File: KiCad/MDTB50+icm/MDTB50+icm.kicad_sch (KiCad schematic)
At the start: 21 parts, among them U1 ICM-45686

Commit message: - DIY PCB fully routed. But it kinda sucks.
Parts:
- renumbered U3 to TP1
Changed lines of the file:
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@@
 		(on_board yes)
 		(dnp no)
-		(property "Reference" "U3"
+		(property "Reference" "TP1"
 			(at 52.07 35.052 0)
 			(effects
@@
 			(project ""
 				(path "/fc39c71d-b4a8-40e7-814c-897ce106e5ba"
-					(reference "U3")
+					(reference "TP1")
 					(unit 1)
 				)

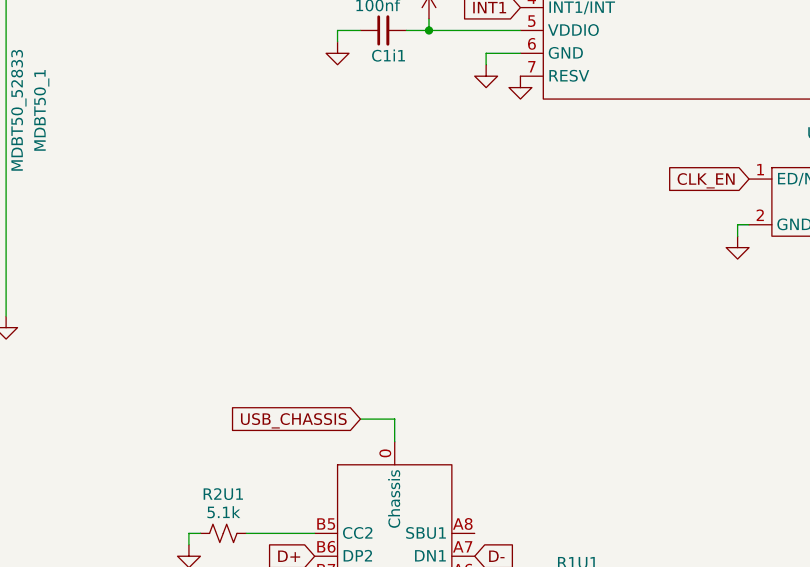
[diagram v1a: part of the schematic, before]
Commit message: - Changed PCB to 4 layer - Added QMC6309 magnetometer
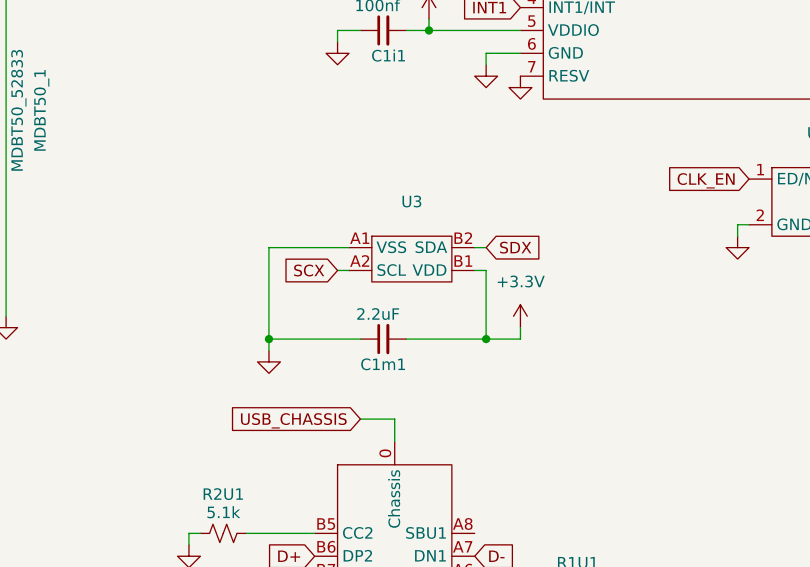
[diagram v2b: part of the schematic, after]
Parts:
- added C1m1: 2.2uF, passive_custom:C_0402_JLC, symbol Device:C_Small
- added U3: ~, mag_custom:QMC6309, symbol mag_custom:QMC6309
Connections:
- net +3.3V: now also C1m1.2, U3.B1 (VDD)
- net GND: now also C1m1.1, U3.A1 (VSS)
- net SCX: now also U3.A2 (SCL)
- net SDX: now also U3.B2 (SDA)

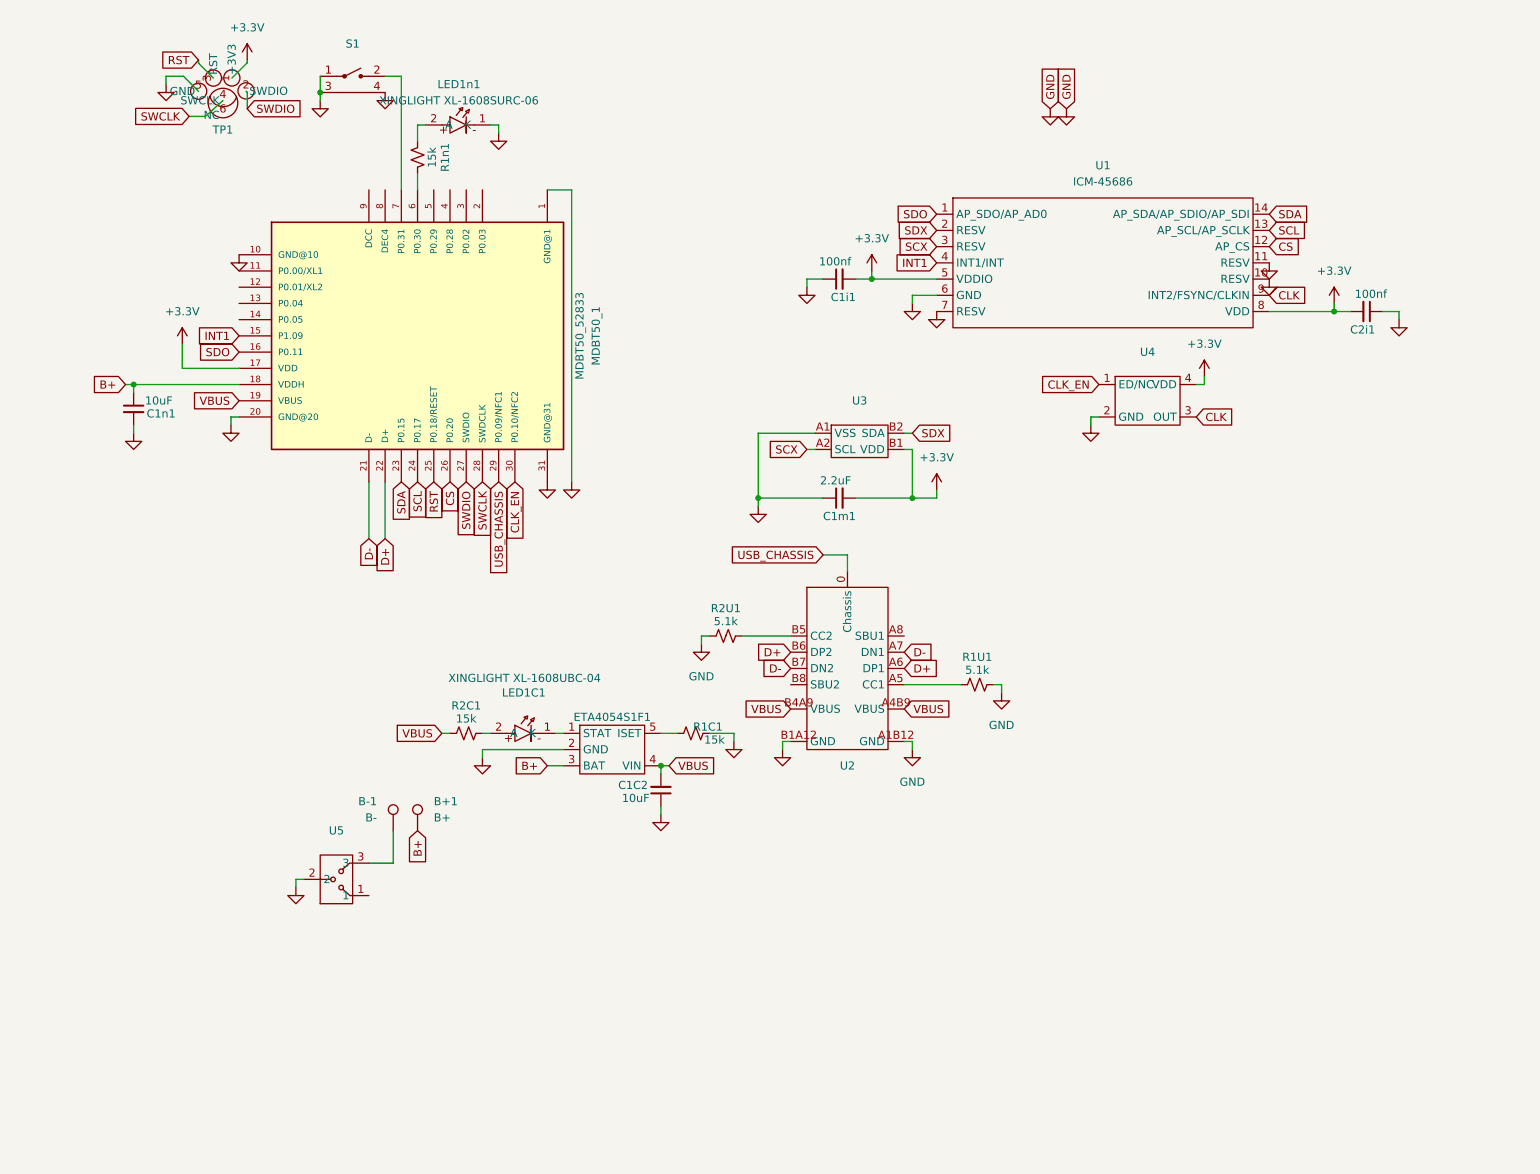
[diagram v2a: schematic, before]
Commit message: - Added external 1.8v regulator, external 3.3v regulator, QMC6309, logic   level shifter for QMC6309, pushbutton power disconnect - Replaced USB C port for better one
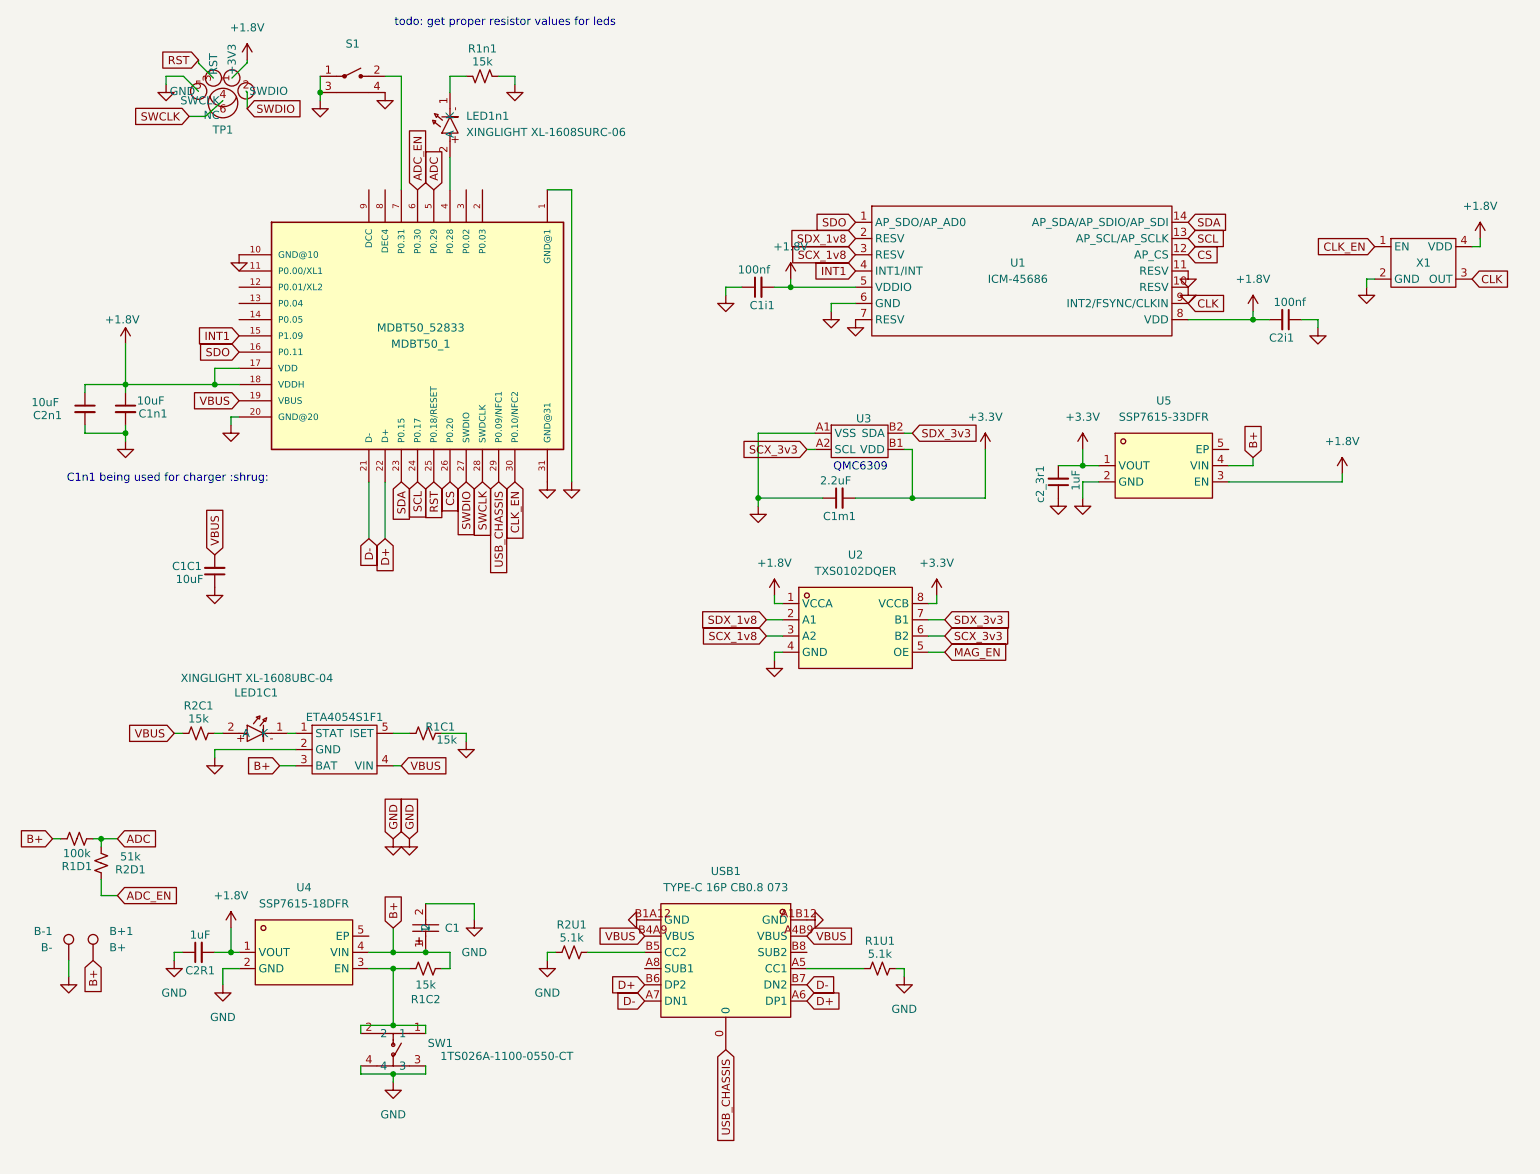
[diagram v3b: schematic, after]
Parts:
- removed C1C2: 10uF, passive_custom:C_0402_JLC, symbol Device:C_Small
- removed U2: ~, USB-C_Custom:HCTL HC-TYPE-C-16P-CB1.0, symbol USB-C_custom:HCTL_HC-TYPE-C-16P-CB1.0
- removed U4: ~, oscillator_custom:HCI 1532H4-32K768JWPDTSNL, symbol oscillator_custom:HCI_1532H4-32K768JWPDTSNL
- removed U5: ~, Switch_Custom:CJS-1200TB, symbol switch-Custom2:Nidec_CJS-1200TB
- added C1: TAJA105K016RNJ, easyeda2kicad:CASE-A_3216, symbol easyeda2kicad:TAJA105K016RNJ
- added C1C1, C2n1: 10uF, passive_custom:C_0402_JLC, symbol Device:C_Small
- added C2R1, c2_3r1: 1uF, passive_custom:C_0402_JLC, symbol Device:C_Small
- added R1C2: 15k, passive_custom:R_0402_JLC, symbol Device:R_Small_US
- added R1D1: 100k, passive_custom:R_0402_JLC, symbol Device:R_Small_US
- added R2D1: 51k, passive_custom:R_0402_JLC, symbol Device:R_Small_US
- added SW1: 1TS026A-1100-0550-CT, easyeda2kicad:SW-SMD_4P-L2.6-W1.6-P0.75-LS3.0, symbol easyeda2kicad:1TS026A-1100-0550-CT
- added U2: TXS0102DQER, Package_SON:X2SON-8_1.4x1mm_P0.35mm, symbol easyeda2kicad:TXS0102DQER
- added U4: SSP7615-18DFR, easyeda2kicad:DFN-4_L1.0-W1.0-P0.65-BL-EP, symbol easyeda2kicad:SSP7615-18DFR
- added U5: SSP7615-33DFR, easyeda2kicad:DFN-4_L1.0-W1.0-P0.65-BL-EP, symbol easyeda2kicad:SSP7615-33DFR
- added USB1: TYPE-C 16P CB0.8 073, easyeda2kicad:USB-C-SMD_TYPE-C-16P-CB0.8-073, symbol easyeda2kicad:TYPE-C16PCB0.8073
- added X1: ~, Crystal:Crystal_SMD_2520-4Pin_2.5x2.0mm, symbol oscillator_custom:SX2M32.768KM20F30TNN
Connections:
- net +3.3V: now also U2.8 (VCCB), U5.1 (VOUT), c2_3r1.2; no longer C1i1.2, C2i1.2, MDBT50_1.17 (VDD), TP1.1 (+3V3), U1.5 (VDDIO), U1.8 (VDD)
- net B+: now also C1.1, R1C2.2, R1D1.2, U4.4 (VIN), U5.4 (VIN); no longer C1n1.1, MDBT50_1.18 (VDDH)
- net CLK: now also X1.3 (OUT)
- net CLK_EN: now also X1.1 (EN)
- net D+: now also USB1.A6 (DP1), USB1.B6 (DP2)
- net D-: now also USB1.A7 (DN1), USB1.B7 (DN2)
- net GND: now also B-1.1, R1n1.1, C1.2, C1C1.1, C2R1.1, C2n1.2, SW1.3, SW1.4, U2.4 (GND), U4.2 (GND), U5.2 (GND), USB1.A1B12 (GND), USB1.B1A12 (GND), X1.2 (GND), c2_3r1.1; no longer LED1n1.1 (K)
- net USB_CHASSIS: now also USB1.0
- net VBUS: now also C1C1.2, USB1.A4B9 (VBUS), USB1.B4A9 (VBUS)
- net at R1U1.1: now also USB1.A5 (CC1)
- net at R2U1.2: now also USB1.B5 (CC2)
- net at MDBT50_1.4 (P0.28): now also LED1n1.2 (A)
- net ADC: now reaches MDBT50_1.5 (P0.29)
- net ADC: now also R1D1.1, R2D1.2
- net ADC_EN: now reaches MDBT50_1.6 (P0.30)
- net ADC_EN: now also R2D1.1; no longer R1n1.1
- net at R1n1.2: now also LED1n1.1 (K); no longer LED1n1.2 (A)
- net SCX renamed SCX_1v8
- net SCX_1v8: now also U2.3 (A2); no longer U3.A2 (SCL)
- net SDX renamed SDX_1v8
- net SDX_1v8: now also U2.2 (A1); no longer U3.B2 (SDA)
- new net: R1C2.1, SW1.1, SW1.2, U4.3 (EN)
- new net +1.8V: C1i1.2, C1n1.1, C2R1.2, C2i1.2, C2n1.1, MDBT50_1.17 (VDD), MDBT50_1.18 (VDDH), TP1.1 (+3V3), U1.5 (VDDIO), U1.8 (VDD), U2.1 (VCCA), U4.1 (VOUT), U5.3 (EN), X1.4 (VDD)
- new net MAG_EN: U2.5 (OE)
- new net SCX_3v3: U2.6 (B2), U3.A2 (SCL)
- new net SDX_3v3: U2.7 (B1), U3.B2 (SDA)
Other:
- note added: "C1n1 being used for charger :shrug:"
- note added: "QMC6309"
- note added: "todo: get proper resistor values for leds"
- moved on the sheet: B+1, B-1, C1i1, C1n1, C2i1, ETA4054S1F1, LED1C1, LED1n1, R1C1, R2C1, U1

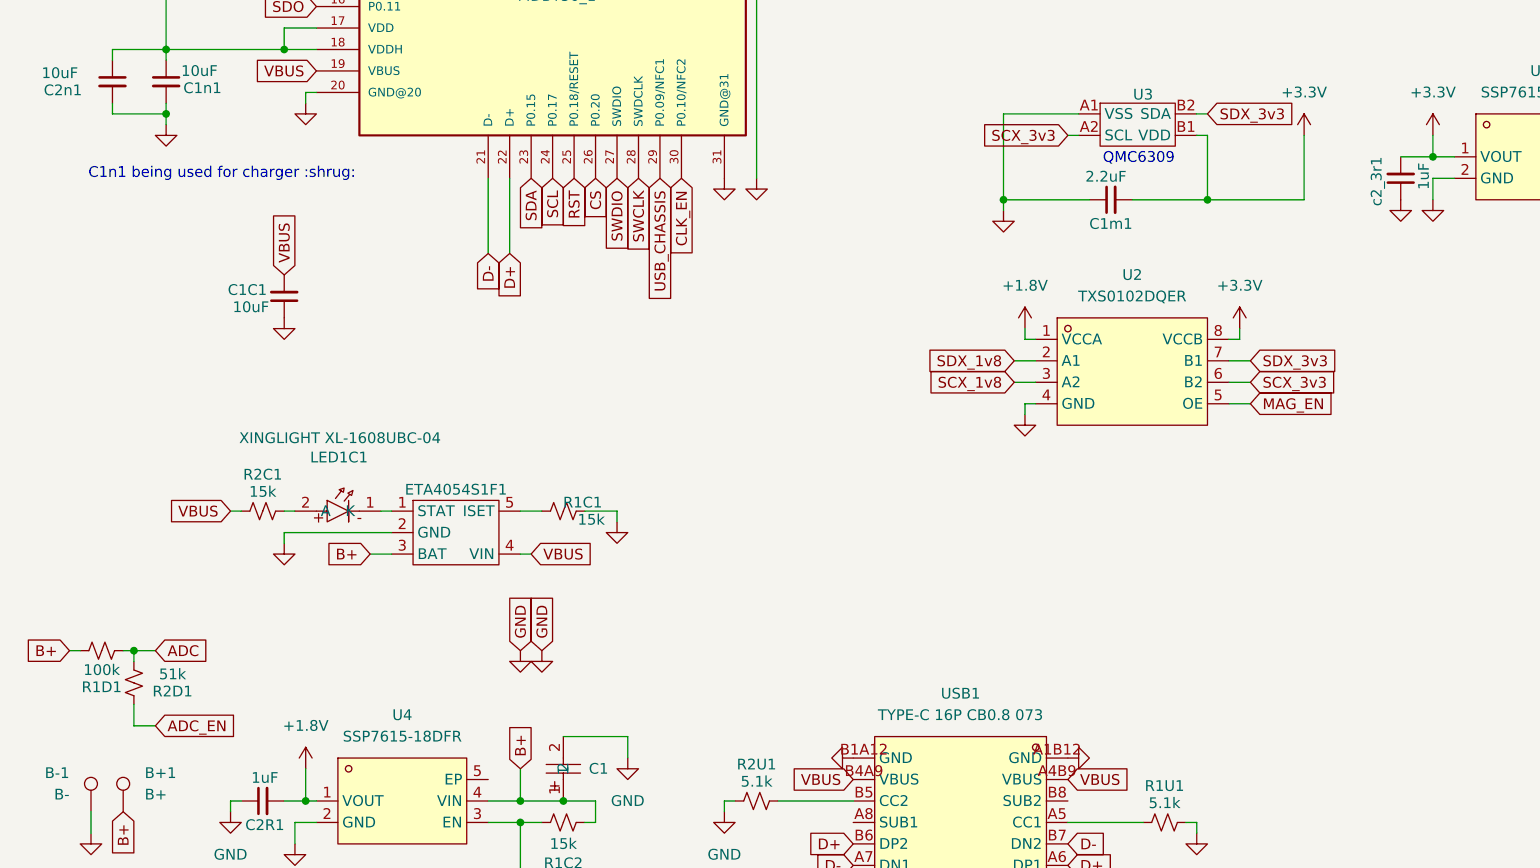
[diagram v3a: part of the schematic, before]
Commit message: - Added ESD protection
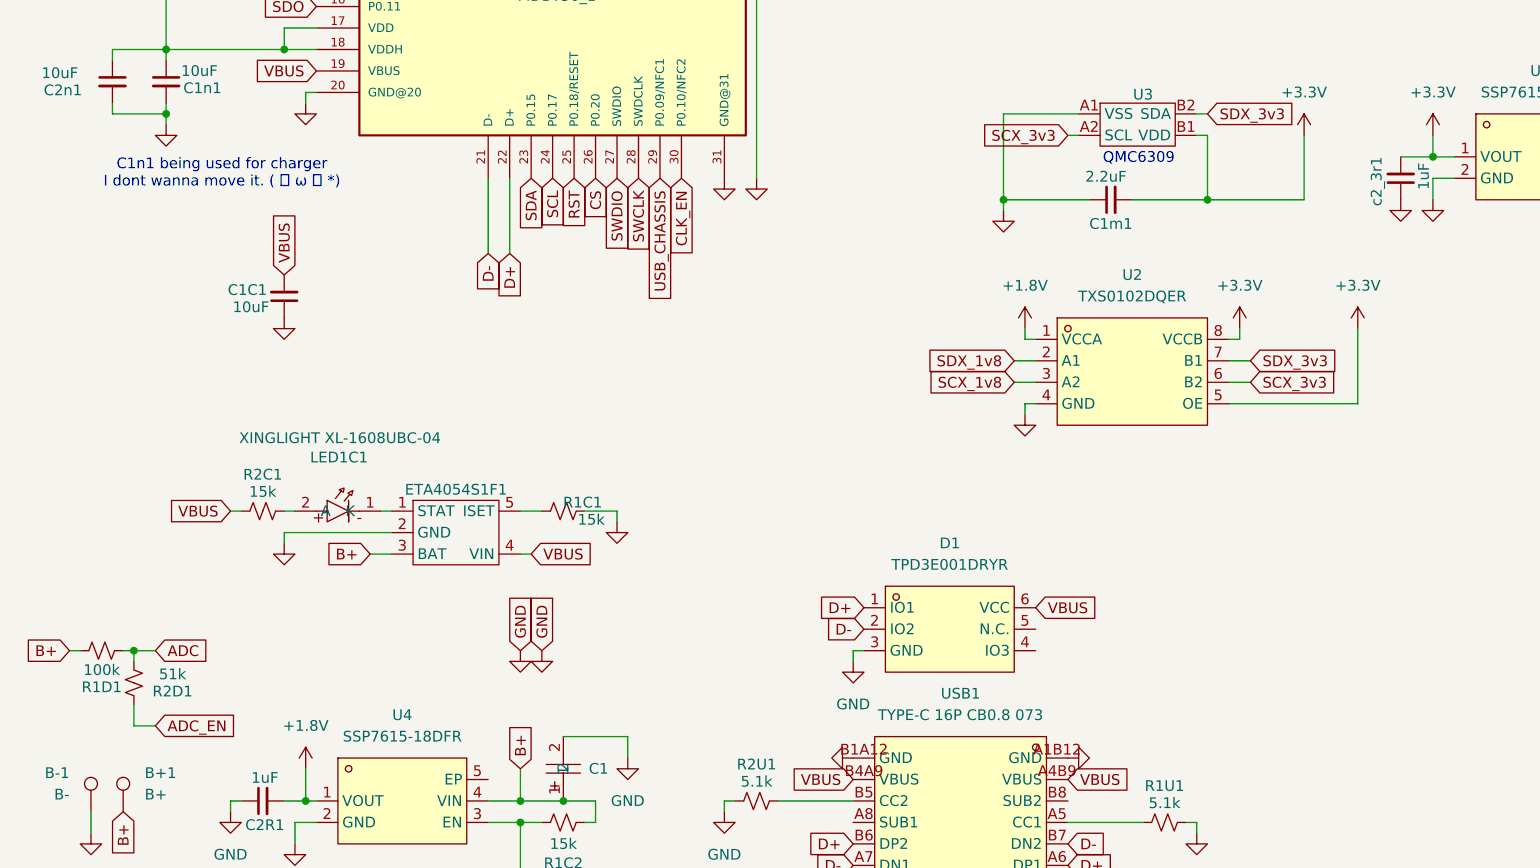
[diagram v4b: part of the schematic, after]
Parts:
- added D1: TPD3E001DRYR, easyeda2kicad:SON-6_L1.5-W1.0-P0.50-BL_SN74LVC1G19DRYR, symbol easyeda2kicad:TPD3E001DRYR
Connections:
- net MAG_EN is gone; now on net +3.3V: U2.5 (OE)
- net D+: now also D1.1 (IO1)
- net D-: now also D1.2 (IO2)
- net GND: now also D1.3 (GND)
- net VBUS: now also D1.6 (VCC)
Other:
- note added: "C1n1 being used for charger I dont wanna move it. ( ⓛ ω ⓛ *)"
- note removed: "C1n1 being used for charger :shrug:"

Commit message: - No more non 90deg angles on components. Yay.
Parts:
- X1: value ~ -> SX2M32.768KM20F30TNN
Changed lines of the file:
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@@
 			)
 		)
-		(property "Value" "~"
-			(at 240.03 50.8 0)
+		(property "Value" "SX2M32.768KM20F30TNN"
+			(at 240.03 47.244 0)
 			(effects
 				(font
@@
 		(on_board yes)
 		(dnp no)
-		(fields_autoplaced yes)
 		(property "Reference" "#PWR026"
 			(at 248.92 55.88 0)
@@
 		)
 		(property "Value" "+1.8V"
-			(at 248.92 46.99 0)
-			(effects
-				(font
+			(at 252.73 50.292 0)
+			(effects
+				(font
